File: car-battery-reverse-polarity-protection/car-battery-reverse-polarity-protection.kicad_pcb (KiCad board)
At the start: 2 copper layers, 45 x 40 mm, 5 parts, among them J1 Battery Connector, J2 Output, K1 Relay_SPDT

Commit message: PCB layout rev 1 complete.
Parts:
- added H1: MountingHole_Pad, MountingHole:MountingHole_3.2mm_M3_Pad, F.Cu at (170.0, 65.5)
- added H2: MountingHole_Pad, MountingHole:MountingHole_3.2mm_M3_Pad, F.Cu at (170.0, 101.5)
- added H3: MountingHole_Pad, MountingHole:MountingHole_3.2mm_M3_Pad, F.Cu at (138.5, 65.5)
- added H4: Logo, ProjectLibrary:rocketry_logo_small_noletters, F.Cu at (169.0, 85.0)
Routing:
- net GND: vias 10 -> 4
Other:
- board size 45 x 40 mm -> 53 x 46 mm
- board text added: "-"

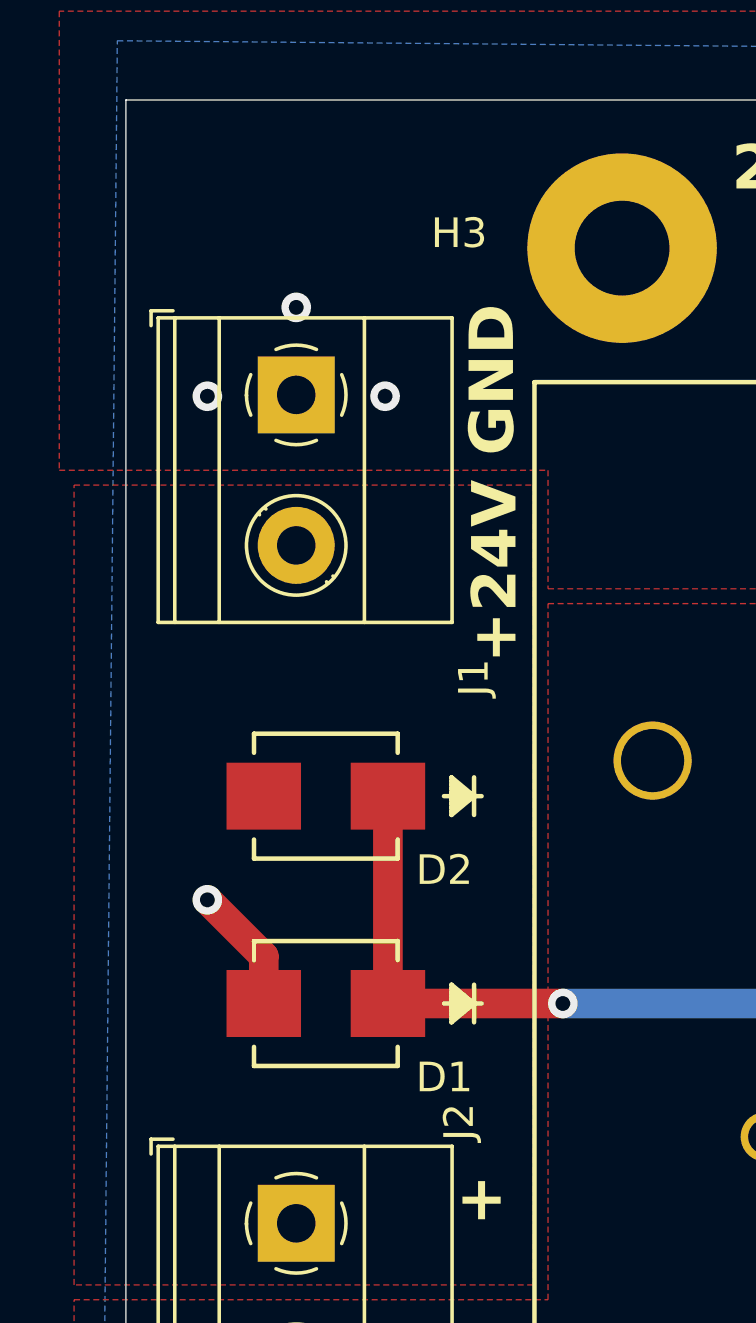
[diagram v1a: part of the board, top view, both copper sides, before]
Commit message: Updated silkscreen.
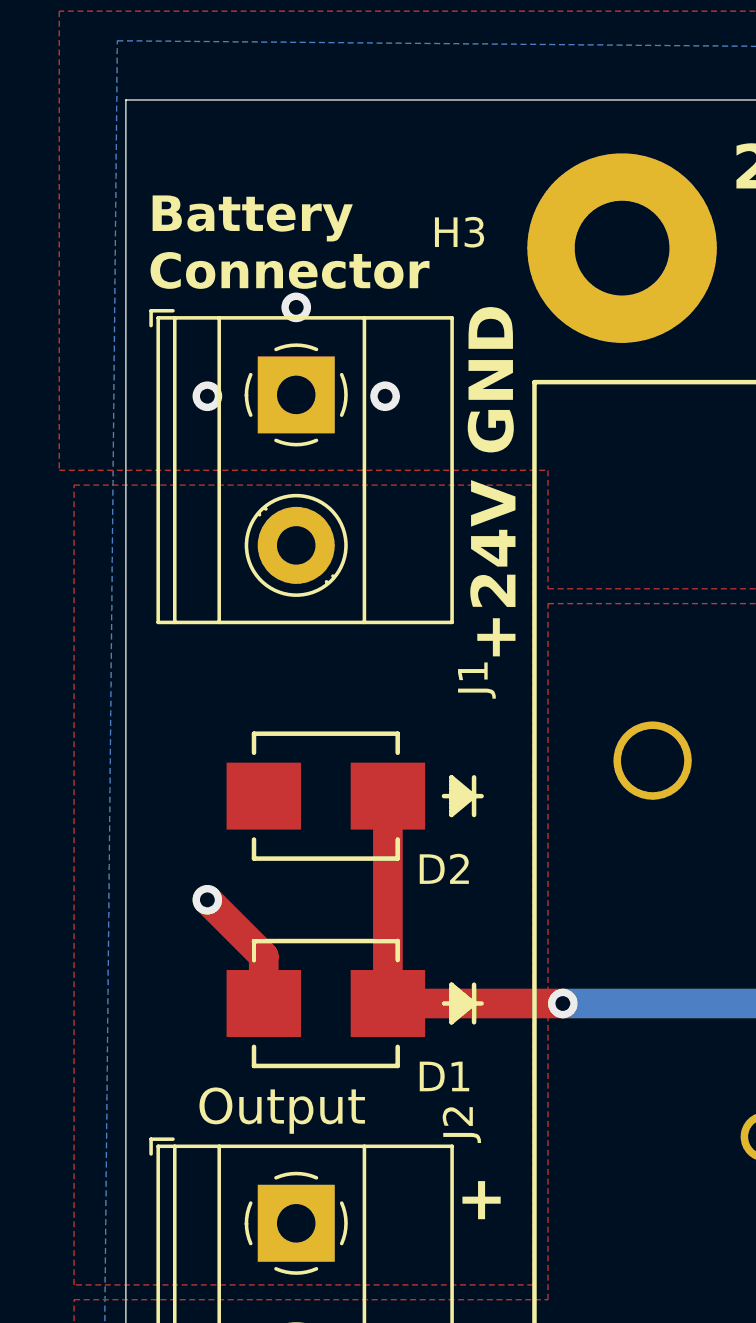
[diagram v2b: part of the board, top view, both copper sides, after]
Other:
- board text added: "Battery Connector"
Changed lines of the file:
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@@
 			(at 9.045 0 180)
 			(layer "F.Fab")
+			(hide yes)
 			(effects
 				(font
@@
 		)
 		(property "Value" "Output"
-			(at -3.42 -0.5 180)
-			(layer "F.Fab")
-			(effects
-				(font
-					(size 1 1)
+			(at -3.92 0.5 180)
+			(layer "F.SilkS")
+			(effects
+				(font
+					(size 1.2 1.2)
 					(thickness 0.15)
 				)
@@
 				(thickness 0.3)
 				(bold yes)
+			)
+			(justify left bottom)
+		)
+	)
+	(gr_text "Battery\nConnector"
+		(at 122.5 67 0)
+		(layer "F.SilkS")
+		(effects
+			(font
+				(size 1.2 1.2)
+				(thickness 0.3)
+				(bold yes)

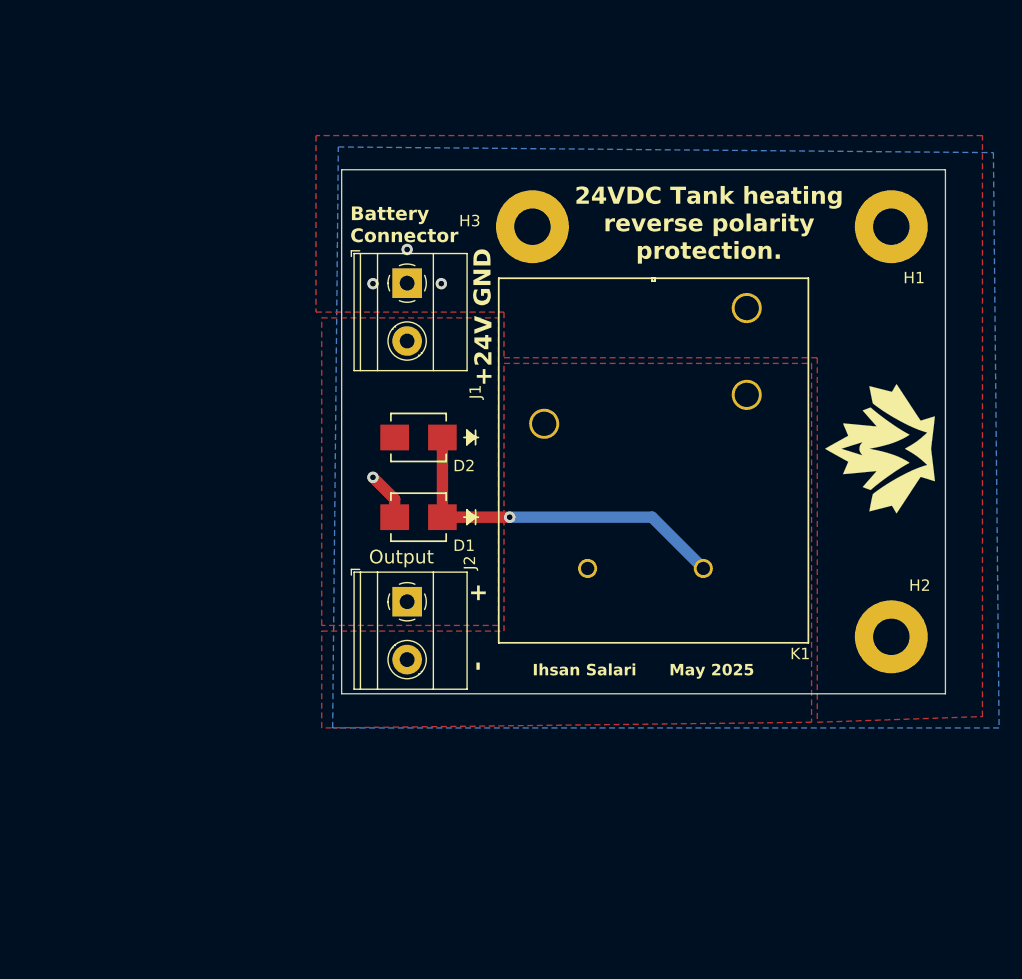
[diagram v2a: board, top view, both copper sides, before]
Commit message: PCB and schematic changes:
- Made board and power traces bigger to meet current requirements.
- Standardized silkscreen labels.
- Updated component values in schematic.
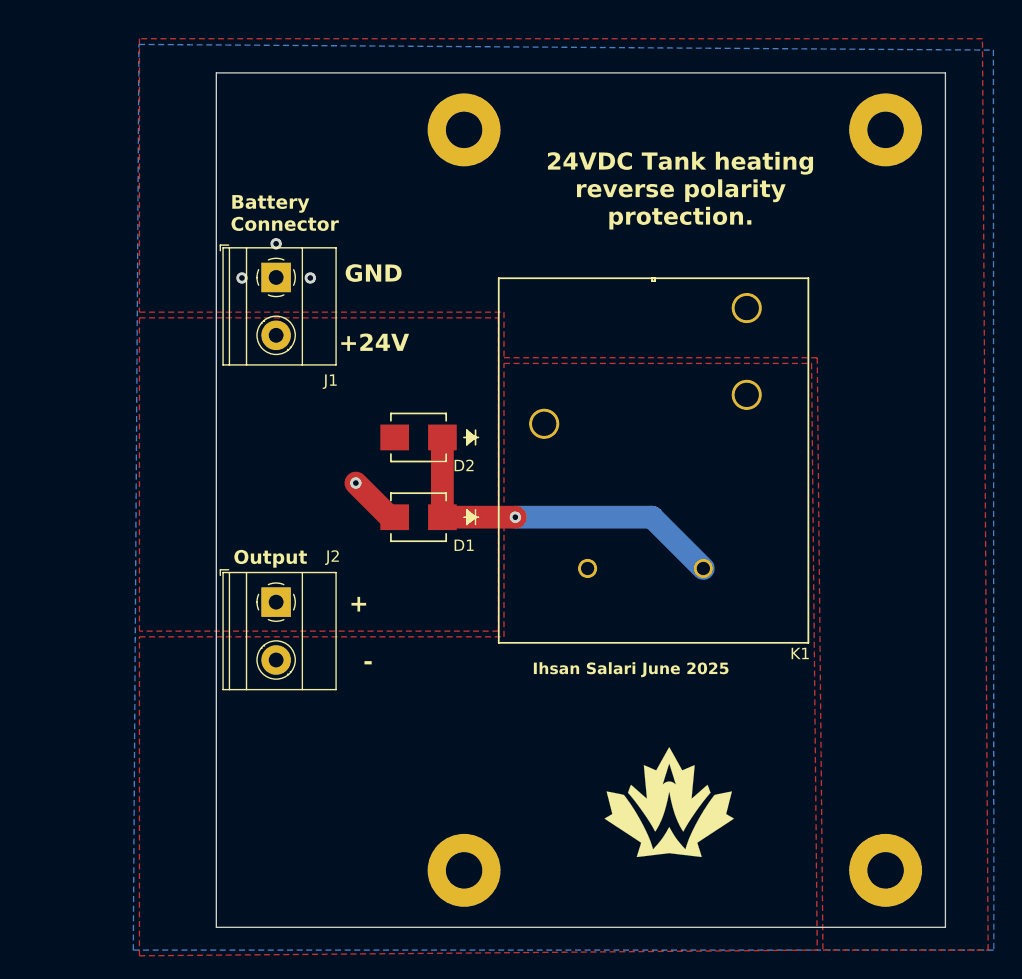
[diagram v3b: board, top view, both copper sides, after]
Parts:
- added H5: MountingHole_Pad, MountingHole:MountingHole_3.2mm_M3_Pad, F.Cu at (132.5, 122.0)
- D1, D2: value D_Schottky -> STPS2L25
- H3: moved to B.Cu
- K1: value Relay_SPDT -> AZ2150-1C
- moved H4 36.1 mm to (150.5, 116.0), turned to 0 degrees
- moved H2 20.5 mm to (169.5, 122.0)
- moved J1 11.5 mm to (116.0, 70.0)
- moved J2 11.5 mm to (116.0, 98.5)
- moved H3 10.4 mm to (132.5, 57.0), turned to 180 degrees
- moved H1 8.51 mm to (169.5, 57.0)
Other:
- board size 53 x 46 mm -> 64 x 75 mm
- board text added: "Ihsan Salari June 2025"
- board text removed: "Ihsan Salari"
- board text removed: "May 2025"

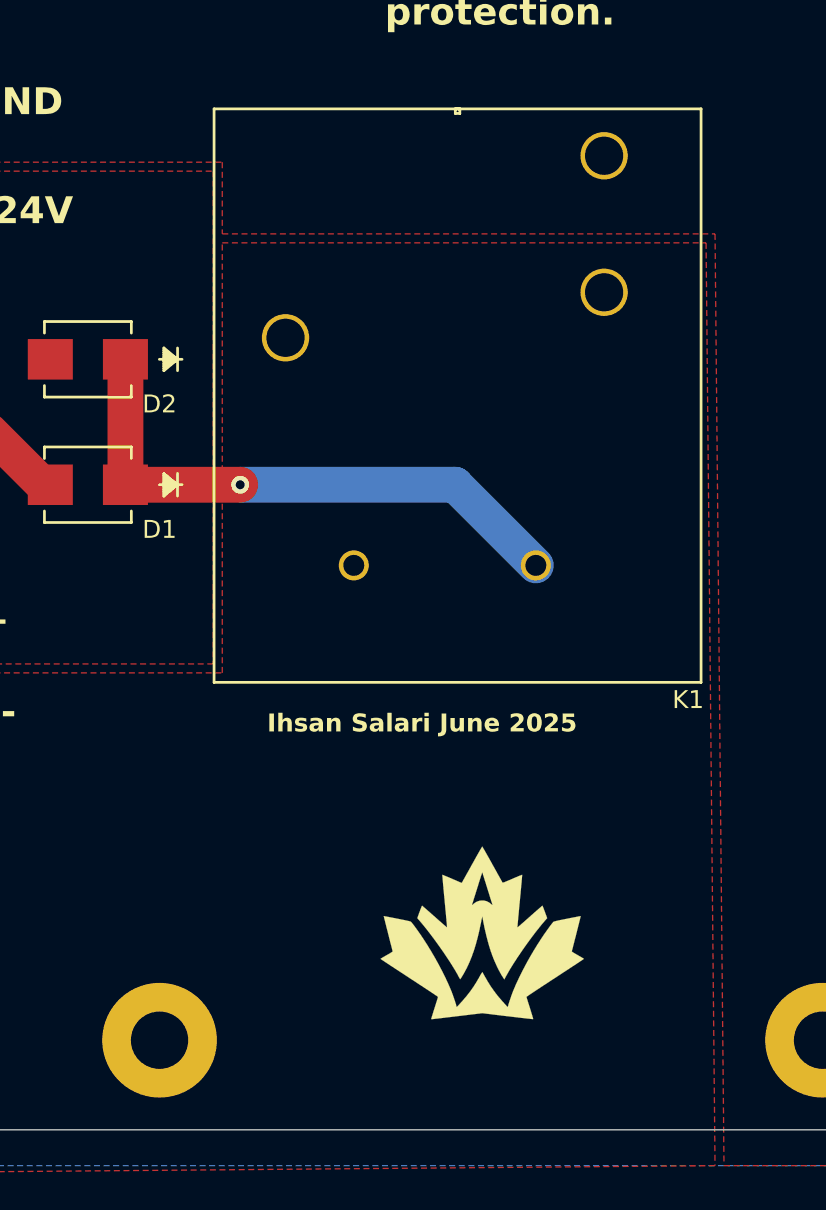
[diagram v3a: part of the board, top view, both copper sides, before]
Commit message: Updates RE: PR
- Updated diode and relay part numbers.
- Updated relay symbol.

Size of board dictated by mounting hole requirement:
- x distance between holes 37mm
- y distance 65 mm
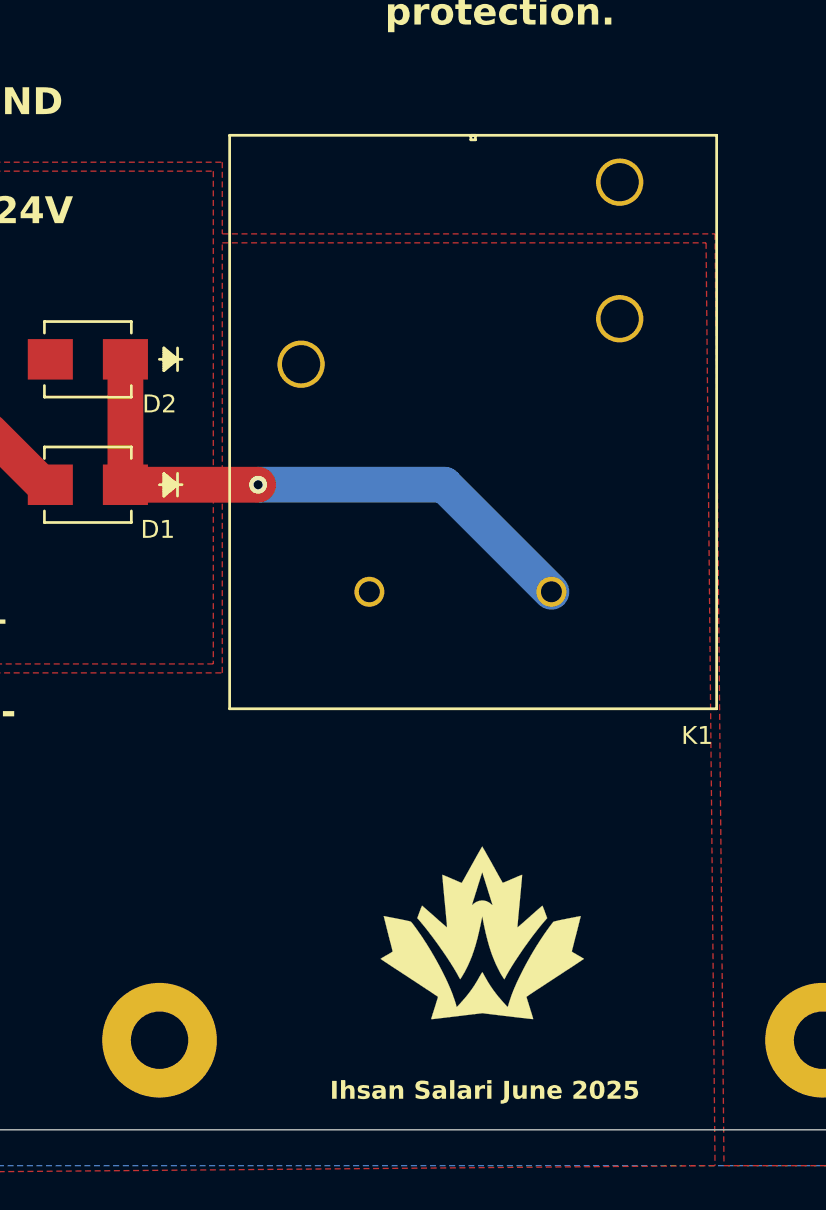
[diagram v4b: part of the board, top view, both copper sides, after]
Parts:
- D1, D2: value STPS2L25 -> STPS2L25U
- K1: value AZ2150-1C -> AZ2150-1AE-24DEF
- moved K1 1.71 mm to (154.4, 97.0)
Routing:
- net /relay_coil: track 31.8 -> 33.2 mm
